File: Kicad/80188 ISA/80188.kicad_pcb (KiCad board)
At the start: 2 copper layers, 143 x 73.9 mm, 24 parts, among them J1 Conn_02x08_Counter_Clockwise, J9 Bus_ISA_8bit, U2 74LS573, U3 74LS573, U4 74LS245, U6 8259, U7 8253, U8 74LS257, Y1 Crystal

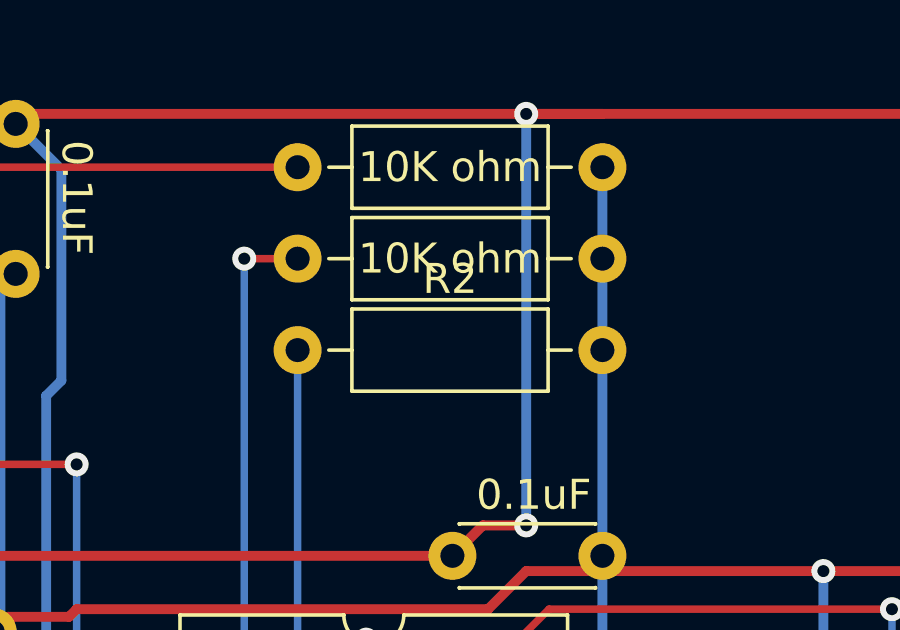
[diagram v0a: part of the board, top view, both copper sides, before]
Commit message: update label on 80188
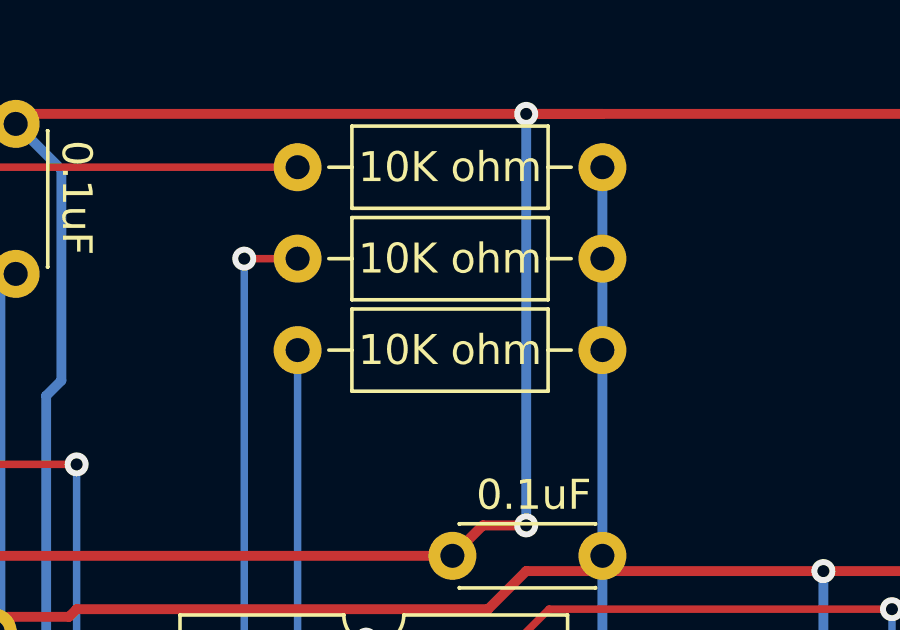
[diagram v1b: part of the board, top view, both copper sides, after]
